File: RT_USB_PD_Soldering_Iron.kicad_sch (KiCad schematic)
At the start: 63 parts, among them J1 USB_C_Receptacle_USB2.0, J2 35RASMT4BHNTRX, SW1 SW_Push, SW2 SW_Push, U1 SPX3819M5-L-3-3, U2 BMI270, U3 DRTR5V0U4S-7, U5 STM32G431Kxxx, U6 TPS25982ONRGET, U7 OPA376AIDCKR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

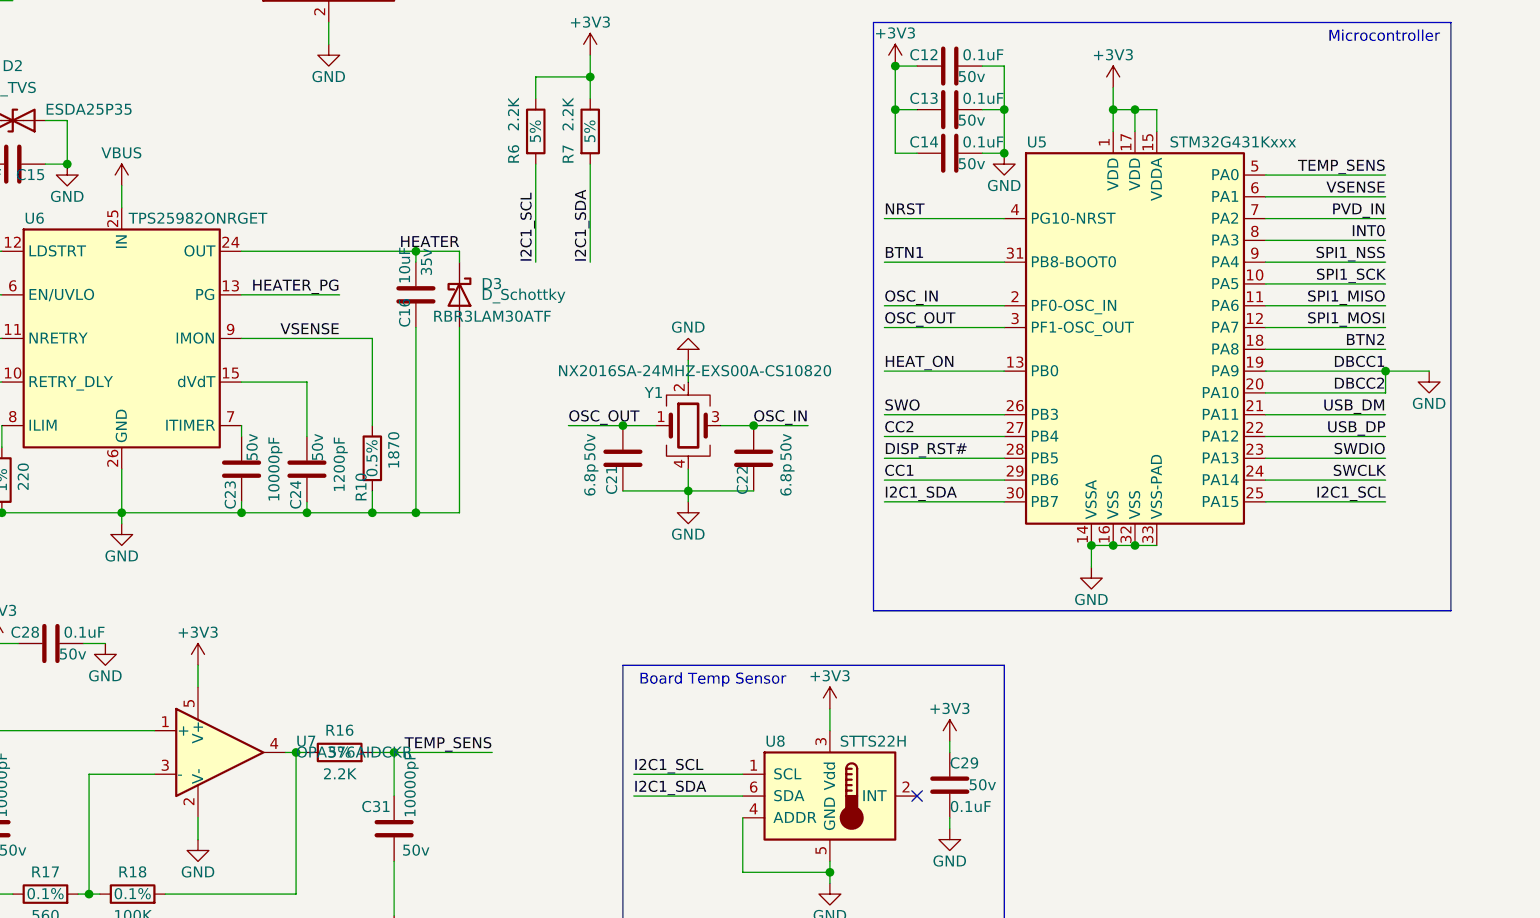
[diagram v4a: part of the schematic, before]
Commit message: change analog pins for improved routing
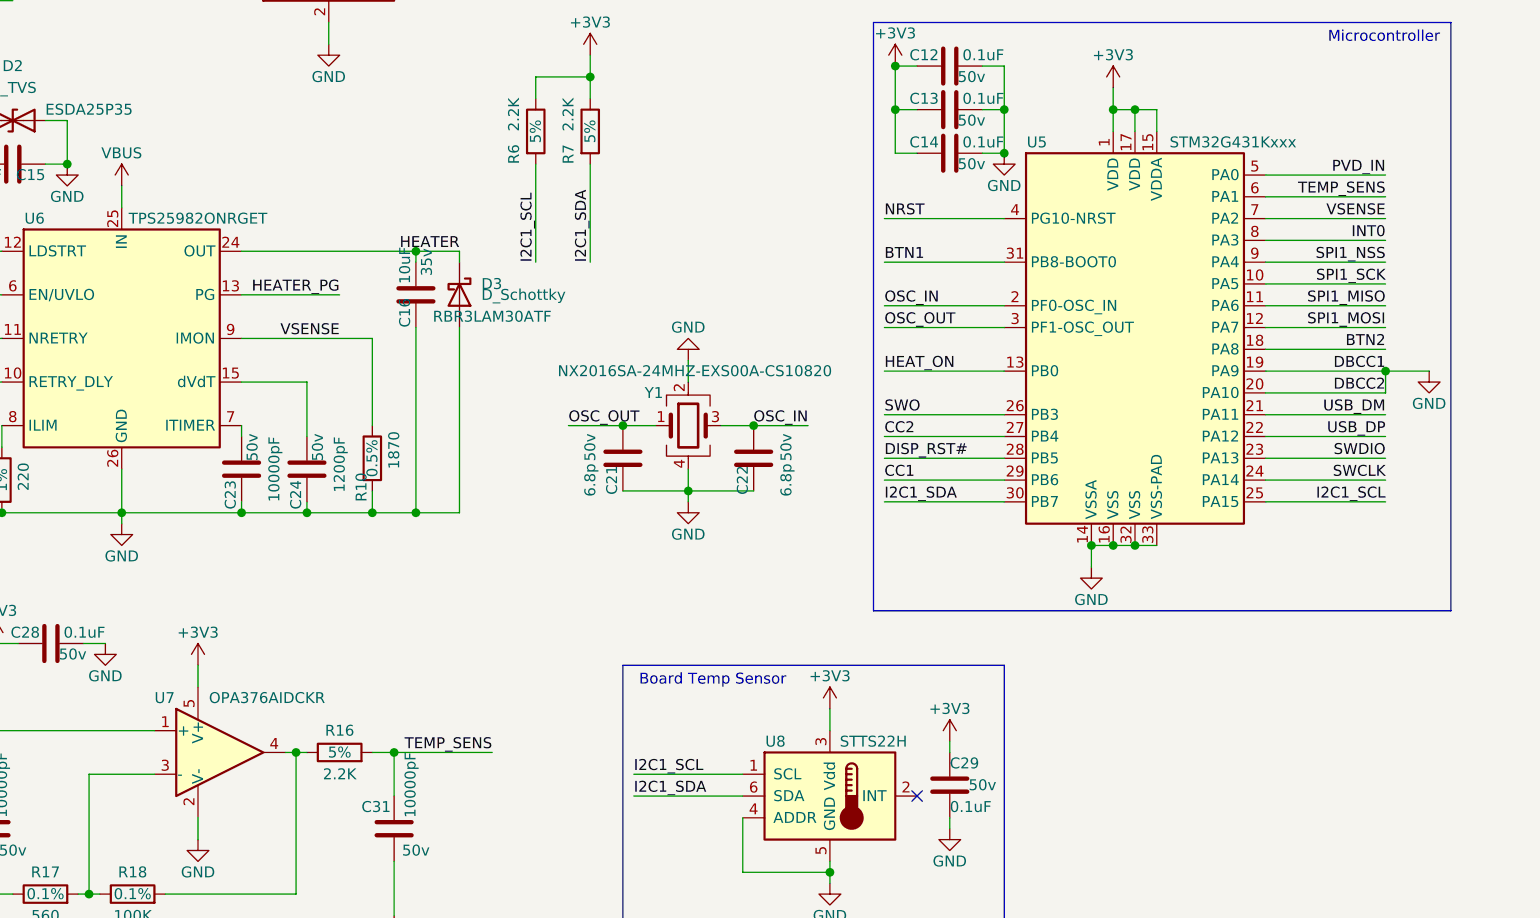
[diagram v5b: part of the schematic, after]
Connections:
- net PVD_IN: now also U5.5 (PA0); no longer U5.7 (PA2)
- net TEMP_SENS: now also U5.6 (PA1); no longer U5.5 (PA0)
- net VSENSE: now also U5.7 (PA2); no longer U5.6 (PA1)
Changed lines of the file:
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@@
   (junction (at 232.41 154.94) (diameter 1.016) (color 0 0 0 0))
   (junction (at 243.84 132.08) (diameter 1.016) (color 0 0 0 0))
+  (no_connect (at 189.23 44.45))
+  (no_connect (at 189.23 41.91))
+  (no_connect (at 189.23 46.99))
+  (no_connect (at 189.23 39.37))
+  (no_connect (at 166.37 49.53))
+  (no_connect (at 147.32 176.53))
+  (no_connect (at 43.18 53.34))
   (no_connect (at 43.18 50.8))
-  (no_connect (at 43.18 53.34))
-  (no_connect (at 189.23 41.91))
-  (no_connect (at 166.37 49.53))
-  (no_connect (at 189.23 44.45))
-  (no_connect (at 189.23 46.99))
-  (no_connect (at 147.32 176.53))
-  (no_connect (at 189.23 39.37))
   (wire (pts (xy 17.78 168.91) (xy 29.21 168.91))
     (stroke (width 0) (type solid) (color 0 0 0 0))
@@
     (effects (font (size 1.27 1.27)) (justify left bottom))
   )
-  (label "TEMP_SENS" (at 201.93 104.14 180)
-    (effects (font (size 1.27 1.27)) (justify right bottom))
-  )
-  (label "VSENSE" (at 201.93 106.68 180)
-    (effects (font (size 1.27 1.27)) (justify right bottom))
-  )
-  (label "PVD_IN" (at 201.93 109.22 180)
+  (label "PVD_IN" (at 201.93 104.14 180)
+    (effects (font (size 1.27 1.27)) (justify right bottom))
+  )
+  (label "TEMP_SENS" (at 201.93 106.68 180)
+    (effects (font (size 1.27 1.27)) (justify right bottom))
+  )
+  (label "VSENSE" (at 201.93 109.22 180)
     (effects (font (size 1.27 1.27)) (justify right bottom))
   )
@@
   (symbol (lib_id "Amplifier_Operational:OPA376xxDCK") (at 66.04 171.45 0) (unit 1)
     (in_bom yes) (on_board yes)
-    (property "Reference" "U7" (id 0) (at 74.93 170.18 0)
-      (effects (font (size 1.27 1.27)) (justify left))
-    )
-    (property "Value" "OPA376AIDCKR" (id 1) (at 74.93 171.45 0)
-      (effects (font (size 1.27 1.27)) (justify left))
-    )
+    (property "Reference" "U7" (id 0) (at 58.42 165.1 0)
+      (effects (font (size 1.27 1.27)) (justify left))
+    )
+    (property "Value" "OPA376AIDCKR" (id 1) (at 64.77 165.1 0)
+      (effects (font (size 1.27 1.27)) (justify left))
+    )

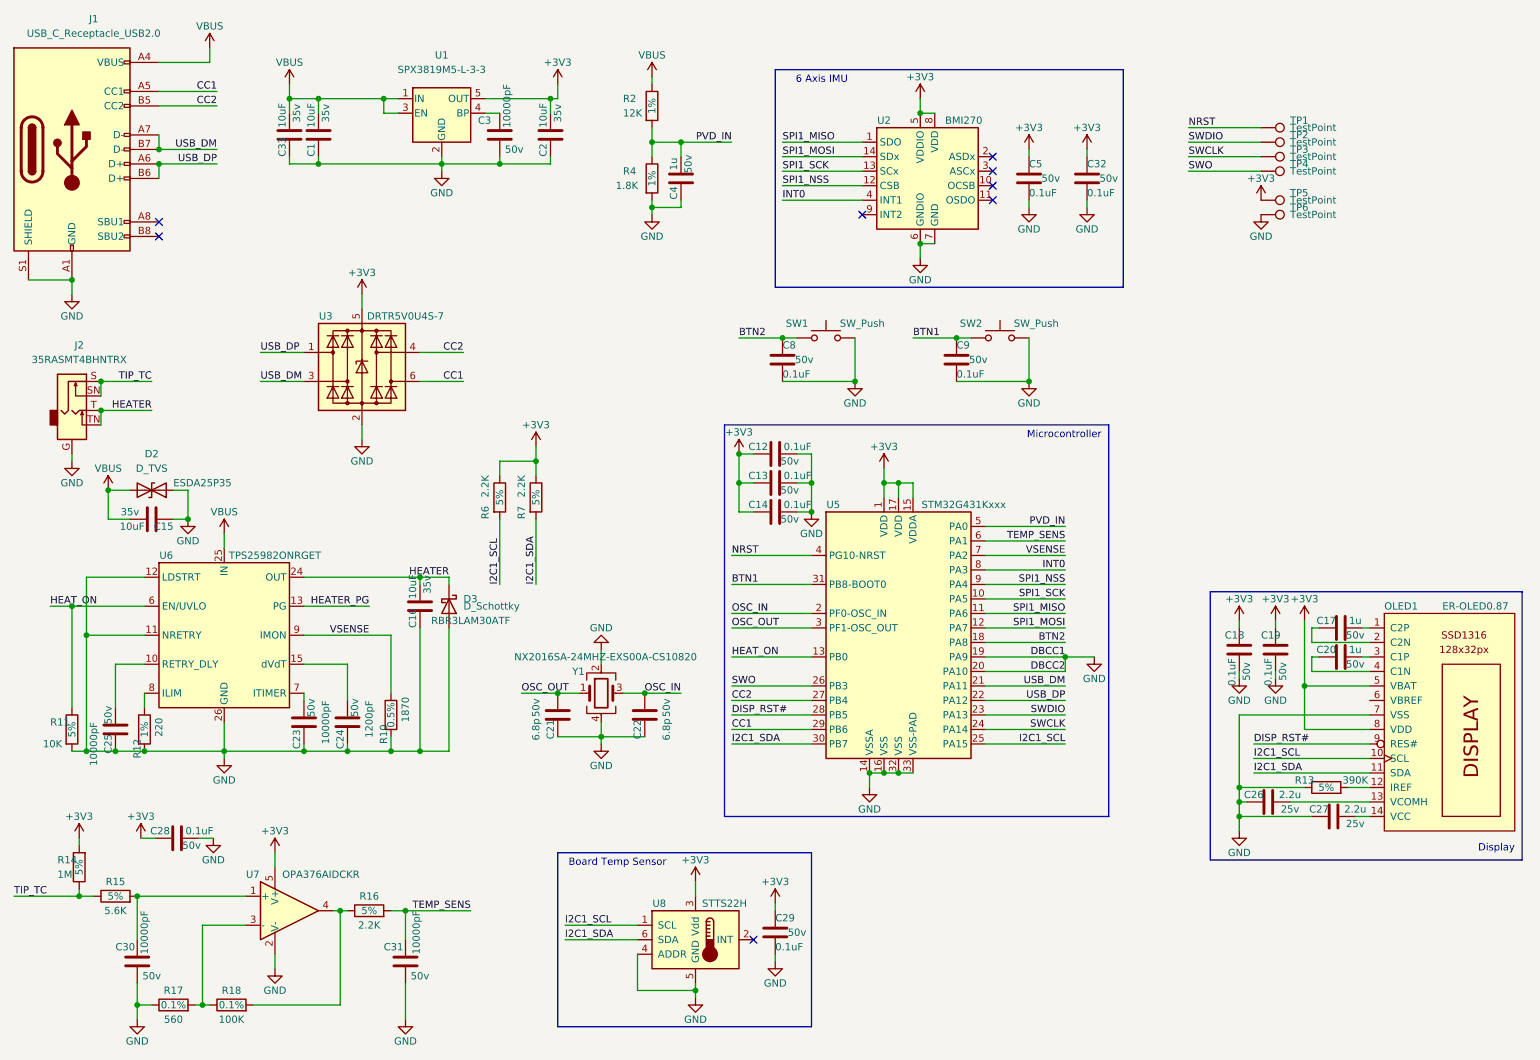
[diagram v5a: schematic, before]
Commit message: update libs/parts
update 0402 footprints for silkscreen
move volate/tolerance to value
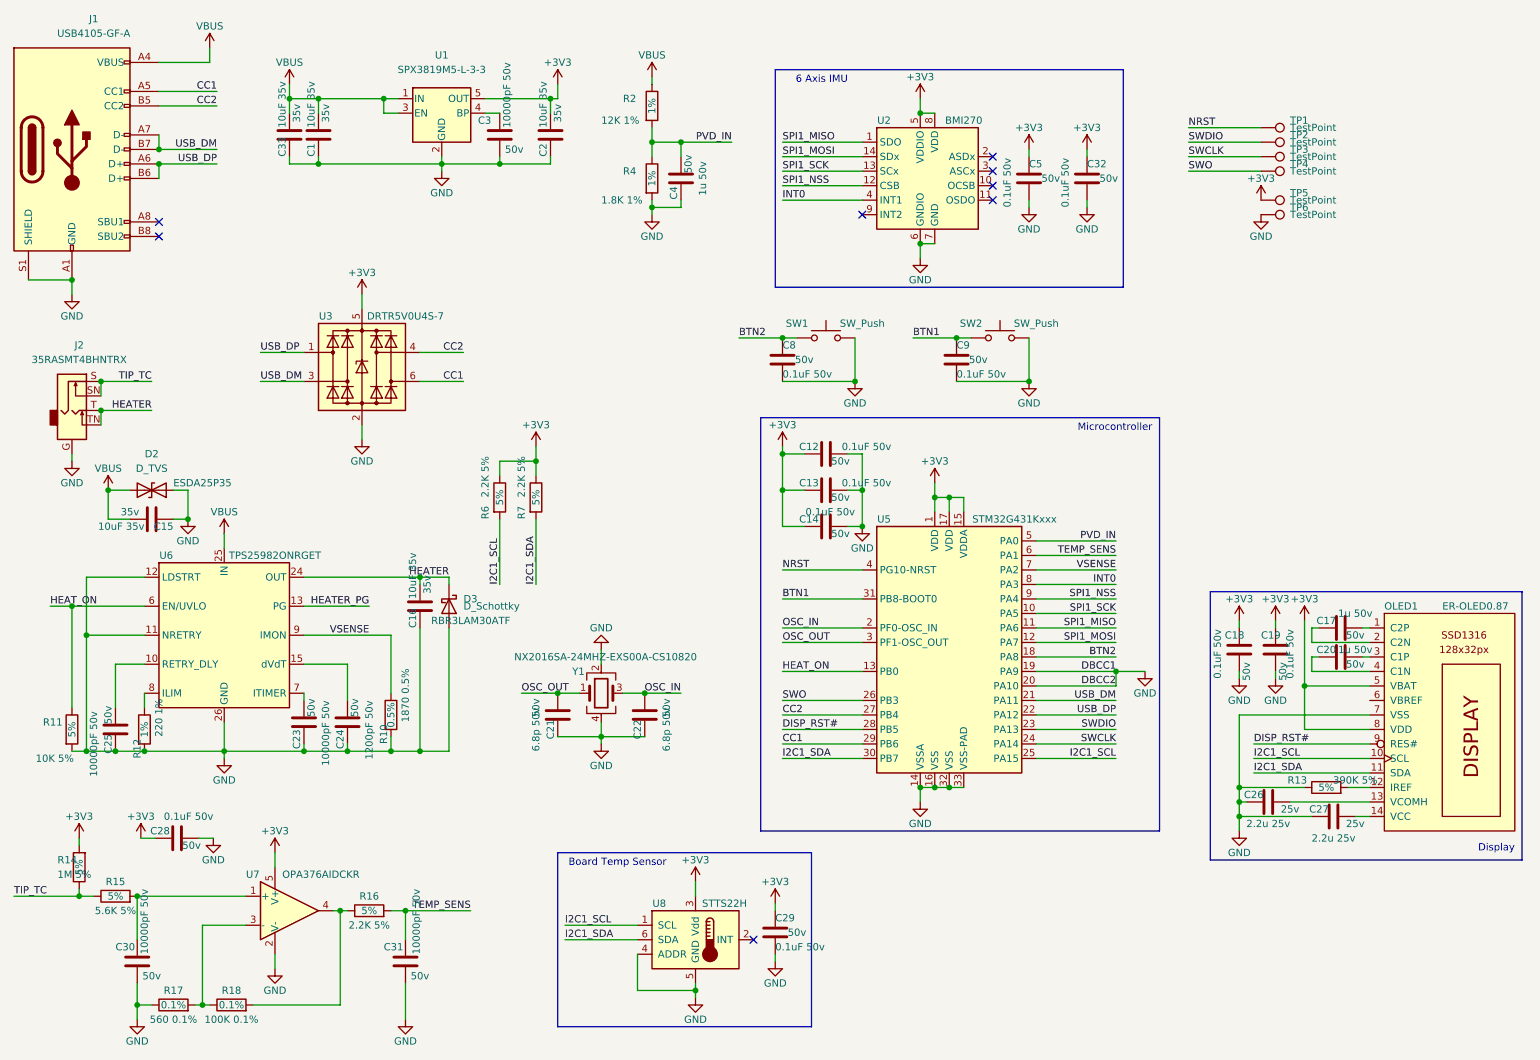
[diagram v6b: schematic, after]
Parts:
- C1, C15, C16, C2, C33: value 10uF -> 10uF 35v
- C12, C13, C14, C18, C19, C28, C29, C32, C5, C8, C9: value 0.1uF -> 0.1uF 50v
- C17, C20, C4: value 1u -> 1u 50v
- C21, C22: value 6.8p -> 6.8p 50v
- C23, C25, C3, C30, C31: value 10000pF -> 10000pF 50v
- C24: value 1200pF -> 1200pF 50v
- C26, C27: value 2.2u -> 2.2u 25v
- J1: value USB_C_Receptacle_USB2.0 -> USB4105-GF-A
- R10: value 1870 -> 1870 0.5%
- R11: value 10K -> 10K 5%
- R12: value 220 -> 220 1%
- R13: value 390K -> 390K 5%
- R14: value 1M -> 1M 5%
- R15: value 5.6K -> 5.6K 5%
- R16, R6, R7: value 2.2K -> 2.2K 5%
- R17: value 560 -> 560 0.1%
- R18: value 100K -> 100K 0.1%
- R2: value 12K -> 12K 1%
- R4: value 1.8K -> 1.8K 1%
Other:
- moved on the sheet: C12, C13, C14, U5
